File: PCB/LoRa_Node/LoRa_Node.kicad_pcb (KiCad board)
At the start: 2 copper layers, 90 x 34 mm, 72 parts, among them IC1 SPX5205M5-L/TR, J1 Conn_01x04_Socket, J2 Conn_01x02_Pin, J3 UF.L, J4 2x5_2.00mm, J6 Conn_01x06_Socket, J7 Conn_01x03_Socket, SW1 SW_SPST, U1 BME280, U2 RFM95W-868S2, U3 STM32F103C8Tx, U4 SIM800L-CORE, U5 SX1308, Y1 12MHz, Y2 32.768kHz

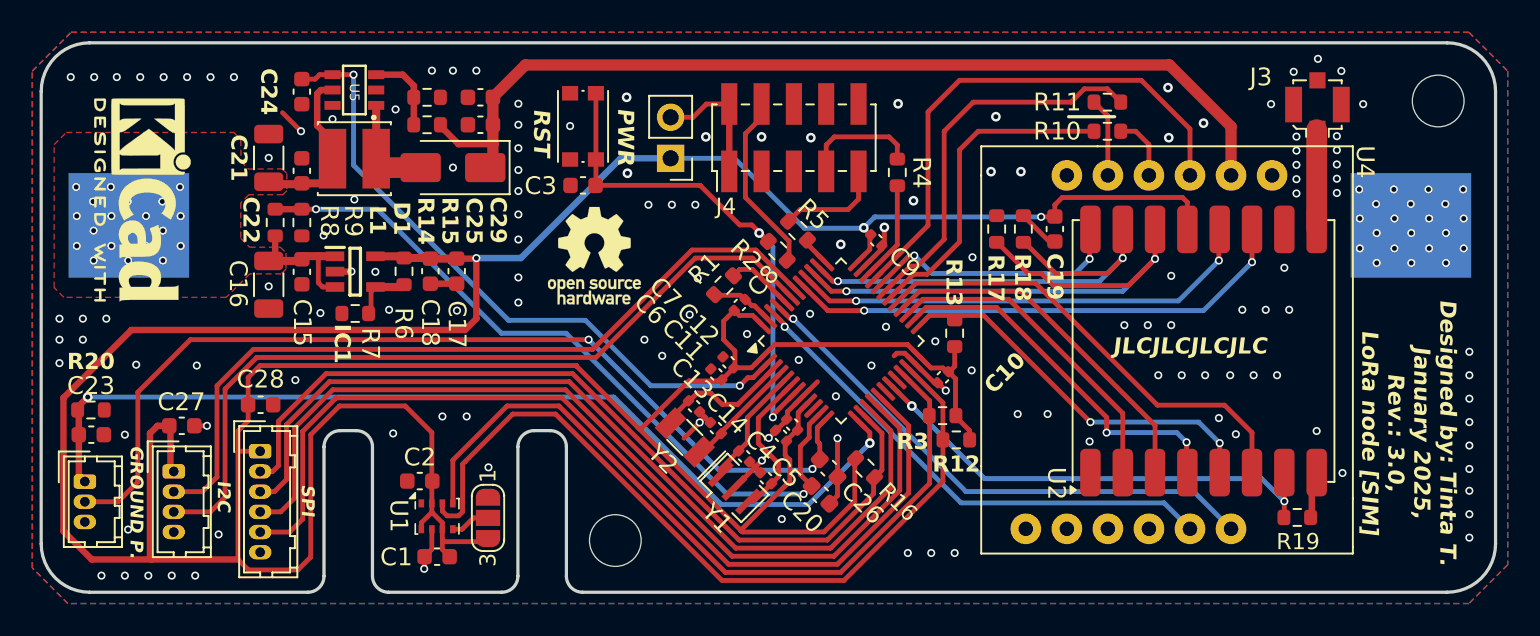
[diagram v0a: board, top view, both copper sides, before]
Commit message: added Docker image for all the server applications
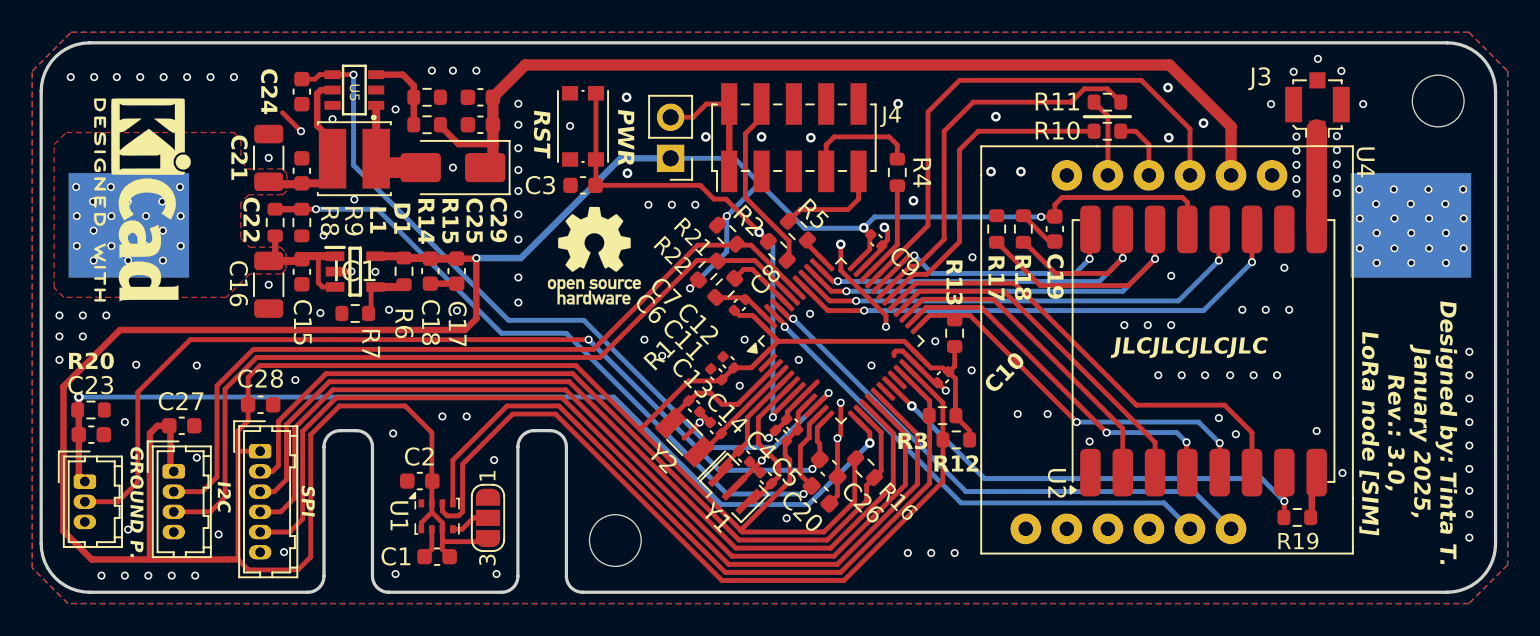
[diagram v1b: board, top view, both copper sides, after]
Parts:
- added R21: 4k7, Resistor_SMD:R_0603_1608Metric, F.Cu at (148.1, 77.6)
- added R22: 4k7, Resistor_SMD:R_0603_1608Metric, F.Cu at (147.0, 79.8)
- moved R1 0.19 mm to (148.0, 80.9)
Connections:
- U3 pad 10: unconnected-(U3-PA0-Pad10) -> /BOOST_EN
- U3 pad 2: /BOOST_EN -> unconnected-(U3-PC13-Pad2)
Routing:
- net +3.3V: track 260.4 -> 268.0 mm, vias 3 -> 5
- net /BOOST_EN: track 40.8 -> 48.3 mm
- net GND: track 40.5 -> 47.8 mm, vias 163 -> 164
- net /MOSI: track 21.7 -> 21.1 mm
- net /SCK: track 23.0 -> 22.5 mm
- net /MISO: track 19.6 -> 19.0 mm

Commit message: PCB modifications, MCU replacement and FW migration
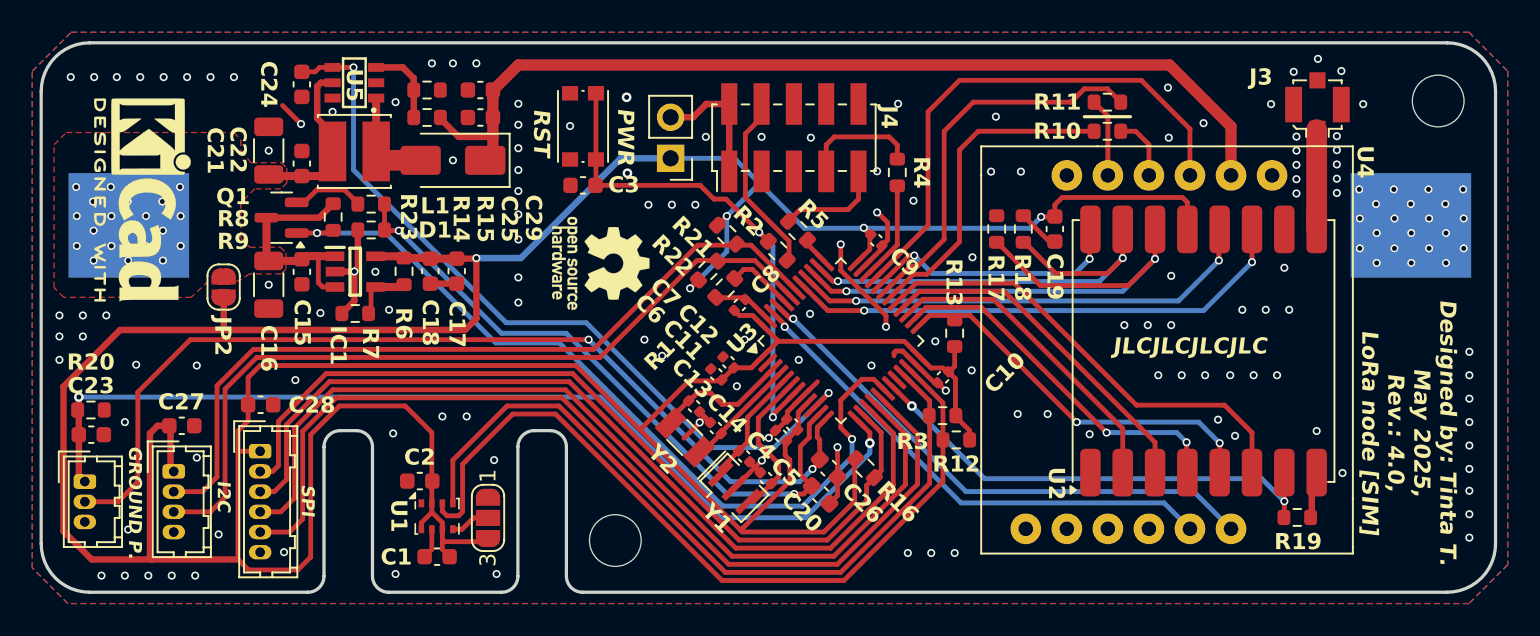
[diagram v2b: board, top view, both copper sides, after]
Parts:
- added JP2: SolderJumper_2_Open, Jumper:SolderJumper-2_P1.3mm_Open_RoundedPad1.0x1.5mm, F.Cu at (117.0, 80.8)
- added Q1: AO3401A, Package_TO_SOT_SMD:SOT-23, F.Cu at (120.6, 76.5)
- added R23: 1k, Resistor_SMD:R_0603_1608Metric, F.Cu at (123.8, 76.5)
- U3: value STM32F103C8Tx -> STM32L151C8T6
- moved R8 6.05 mm to (126.1, 75.7), turned to 180 degrees
- moved R9 4.31 mm to (126.1, 77.3), turned to 0 degrees
- moved REF** 0.62 mm to (140.3, 79.3), turned to -90 degrees
- moved C21 0.45 mm to (119.8, 72.4)
- moved C22 0.45 mm to (121.8, 73.2)
- moved C25 0.45 mm to (132.9, 68.6)
- moved C29 0.45 mm to (132.9, 70.3)
- moved D1 0.45 mm to (131.2, 73.0)
- moved L1 0.45 mm to (125.1, 72.4)
- moved R14 0.45 mm to (129.6, 70.3)
- moved R15 0.45 mm to (129.6, 68.6)
- moved U5 0.45 mm to (125.1, 68.2)
- moved C24 0.45 mm to (121.8, 68.3)
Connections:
- R8 pad 2: +Vbat -> Net-(Q1-S)
- U3 pad 18: unconnected-(U3-PB0-Pad18) -> /D_VBAT_EN
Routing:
- net /D_VBAT_EN: track 0.00 -> 51.1 mm, vias 0 -> 2
- net +Vbat: track 18.2 -> 25.0 mm
- net /AN_BAT: track 45.9 -> 40.2 mm
- net Net-(Q1-S): track 0.00 -> 4.49 mm
- net GND: track 47.8 -> 51.7 mm, vias 164 -> 160
- net +3.3V: track 268.0 -> 270.1 mm
- net /EHUM_PWR: track 61.2 -> 62.2 mm
- net /BOOST_EN: track 48.3 -> 48.9 mm
- net /AN_E_HUM: track 59.3 -> 59.9 mm
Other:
- board text added: "Designed by: Tinta T. May 2025, Rev.: 4.0, LoRa node [SIM]"
- board text removed: "Designed by: Tinta T. January 2025, Rev.: 3.0, LoRa node [SIM]"

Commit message: update
working code for new mcu, current consumption still 900uA
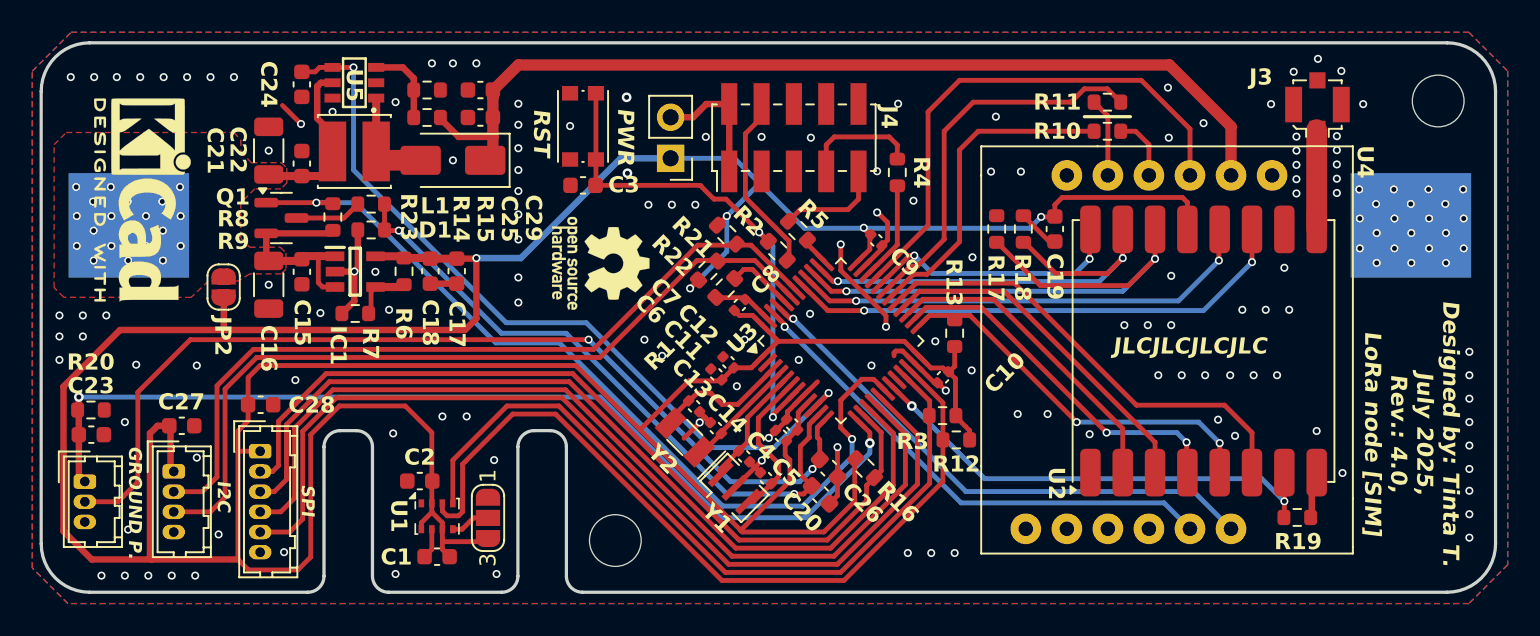
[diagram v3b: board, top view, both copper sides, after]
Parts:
- R8, R9: value 500k -> 100
- turned Q1 to 0 degrees
- turned R23 to -90 degrees
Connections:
- Q1 pad 2: Net-(Q1-S) -> +Vbat
- Q1 pad 3: +Vbat -> Net-(Q1-D)
- R8 pad 2: Net-(Q1-S) -> Net-(Q1-D)
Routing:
- net Net-(Q1-S): track 4.49 -> 0.00 mm
- net Net-(Q1-D): track 0.00 -> 4.20 mm
- net /D_VBAT_EN: track 51.1 -> 53.8 mm
- net +Vbat: track 25.0 -> 24.2 mm
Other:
- board text added: "Designed by: Tinta T. July 2025, Rev.: 4.0, LoRa node [SIM]"
- board text removed: "Designed by: Tinta T. May 2025, Rev.: 4.0, LoRa node [SIM]"

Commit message: update
updated PCB
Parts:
- moved C19 0.27 mm to (168.2, 77.2), turned to 90 degrees
- moved U4 0.12 mm to (181.8, 73.8)
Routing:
- net GND: track 51.7 -> 49.1 mm, vias 160 -> 161
- net +3.3V: track 270.1 -> 272.3 mm

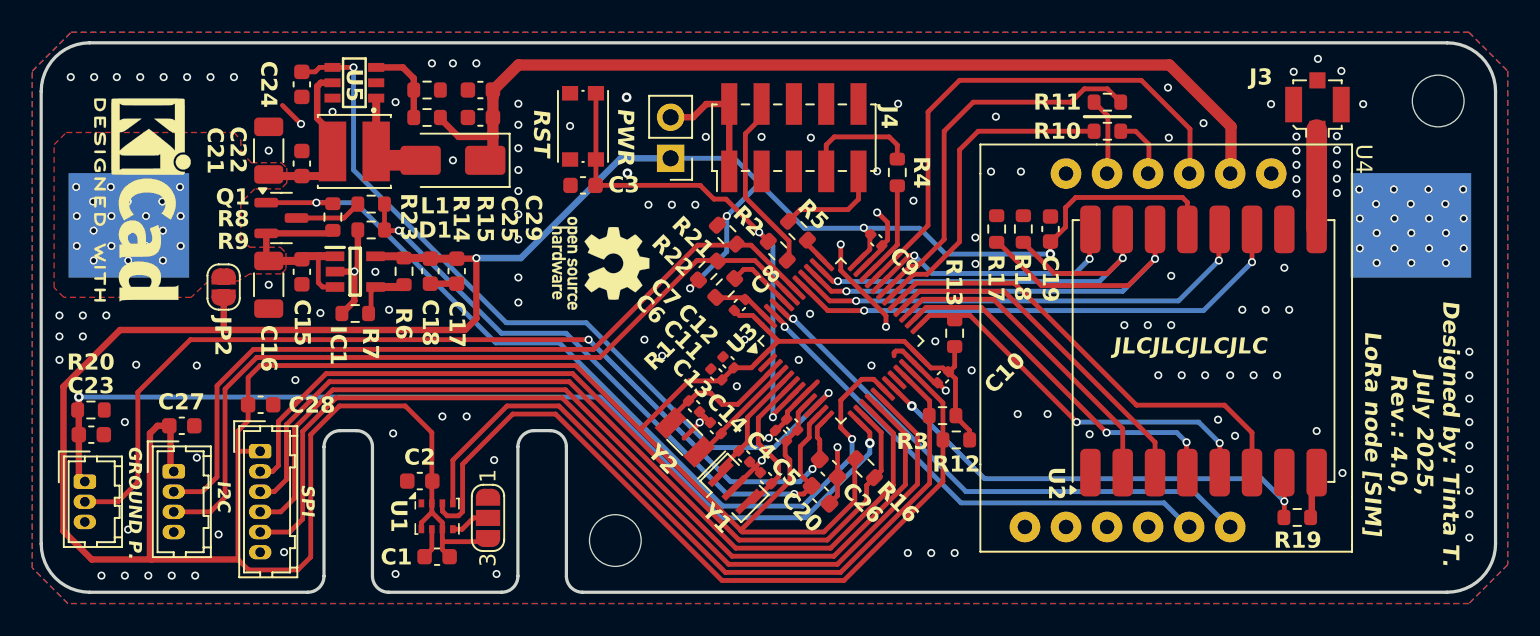
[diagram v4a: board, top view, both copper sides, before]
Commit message: Update
firmware current optimisation
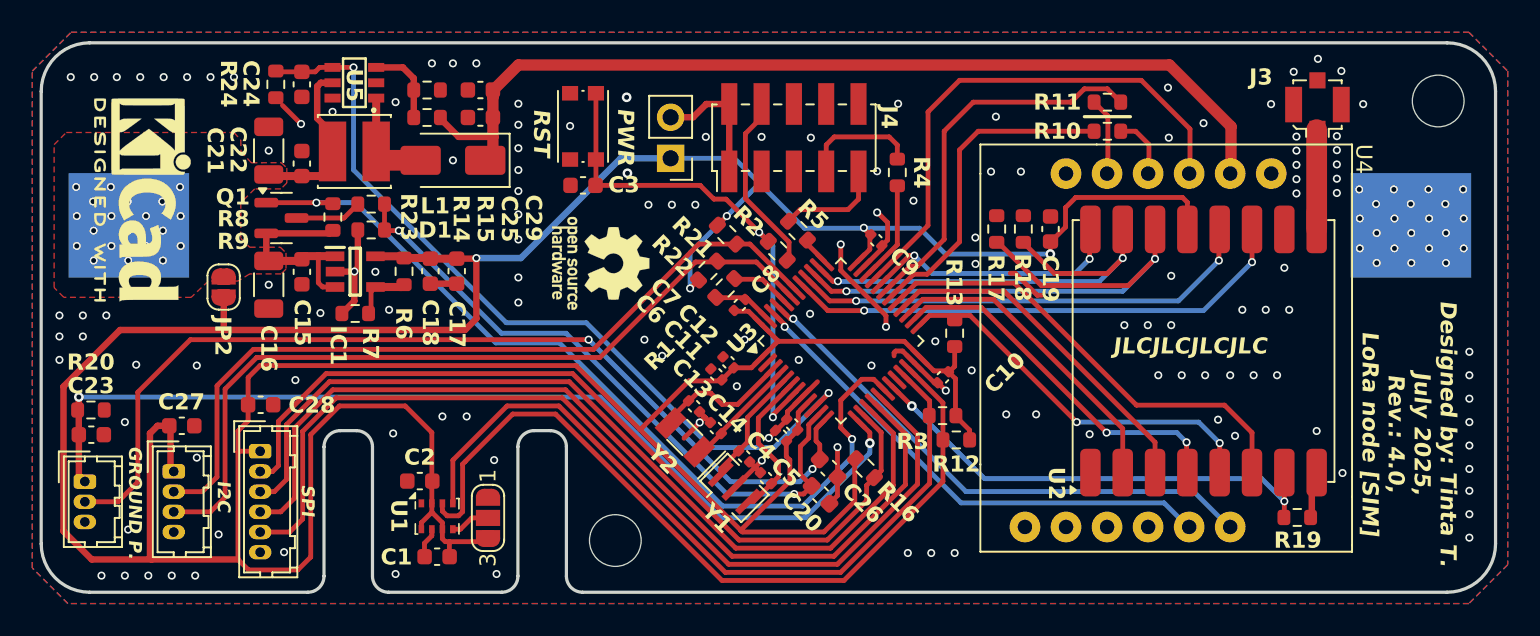
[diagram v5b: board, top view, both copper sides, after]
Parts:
- added R24: 10k, Resistor_SMD:R_0603_1608Metric, F.Cu at (120.2, 68.3)
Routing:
- net GND: track 49.1 -> 51.6 mm
- net /BOOST_EN: track 48.9 -> 50.6 mm
- net Net-(U3-BOOT0): track 4.19 -> 3.31 mm
